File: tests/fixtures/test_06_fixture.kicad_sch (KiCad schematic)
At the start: 4 parts, among them SW1 Desc, SW2 Desc

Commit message: updated test 06 fixtures with LocLoad field
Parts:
- BT1: CInfo |(0,0,0)S40 -> (none); LocLoad (none) -> (0,0,0)S40
- FH1: CInfo |(10,0,0)R40 -> (none); LocLoad (none) -> (10,0,0)R40
- SW1: CInfo |(5,10,-2)R20 -> (none); LocLoad (none) -> (5,10,-2)R20
- SW2: CInfo |(5,10,2)R20 -> (none); LocLoad (none) -> (5,10,2)R20
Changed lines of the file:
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@@
 			)
 		)
-		(property "CInfo" "|(0,0,0)S40"
+		(property "LocLoad" "(0,0,0)S40"
 			(at 59.69 114.3 0)
 			(effects
@@
 			)
 		)
-		(property "CInfo" "|(5,10,-2)R20"
+		(property "LocLoad" "(5,10,-2)R20"
 			(at 138.43 53.34 0)
 			(effects
@@
 			)
 		)
-		(property "CInfo" "|(5,10,2)R20"
+		(property "LocLoad" "(5,10,2)R20"
 			(at 139.7 76.2 0)
 			(effects
@@
 		(dnp no)
 		(fields_autoplaced yes)
-		(property "Reference" "|(0,0,10)G"
+		(property "Reference" "GND"
 			(at 59.69 133.35 0)
 			(effects
@@
 		)
 		(property "Description" "Power symbol creates a global label with name \"GND\" , ground"
+			(at 59.69 127 0)
+			(effects
+				(font
+					(size 1.27 1.27)
+				)
+				(hide yes)
+			)
+		)
+		(property "LocLoad" "(0,0,10)G"
 			(at 59.69 127 0)
 			(effects
@@
 			(project ""
 				(path "/6f32b1c6-d0dc-4a69-b565-c121d7833096"
-					(reference "|(0,0,10)G")
+					(reference "GND")
 					(unit 1)
 				)
@@
 			)
 		)
-		(property "CInfo" "|(10,0,0)R40"
+		(property "LocLoad" "(10,0,0)R40"
 			(at 87.63 78.74 90)
 			(effects

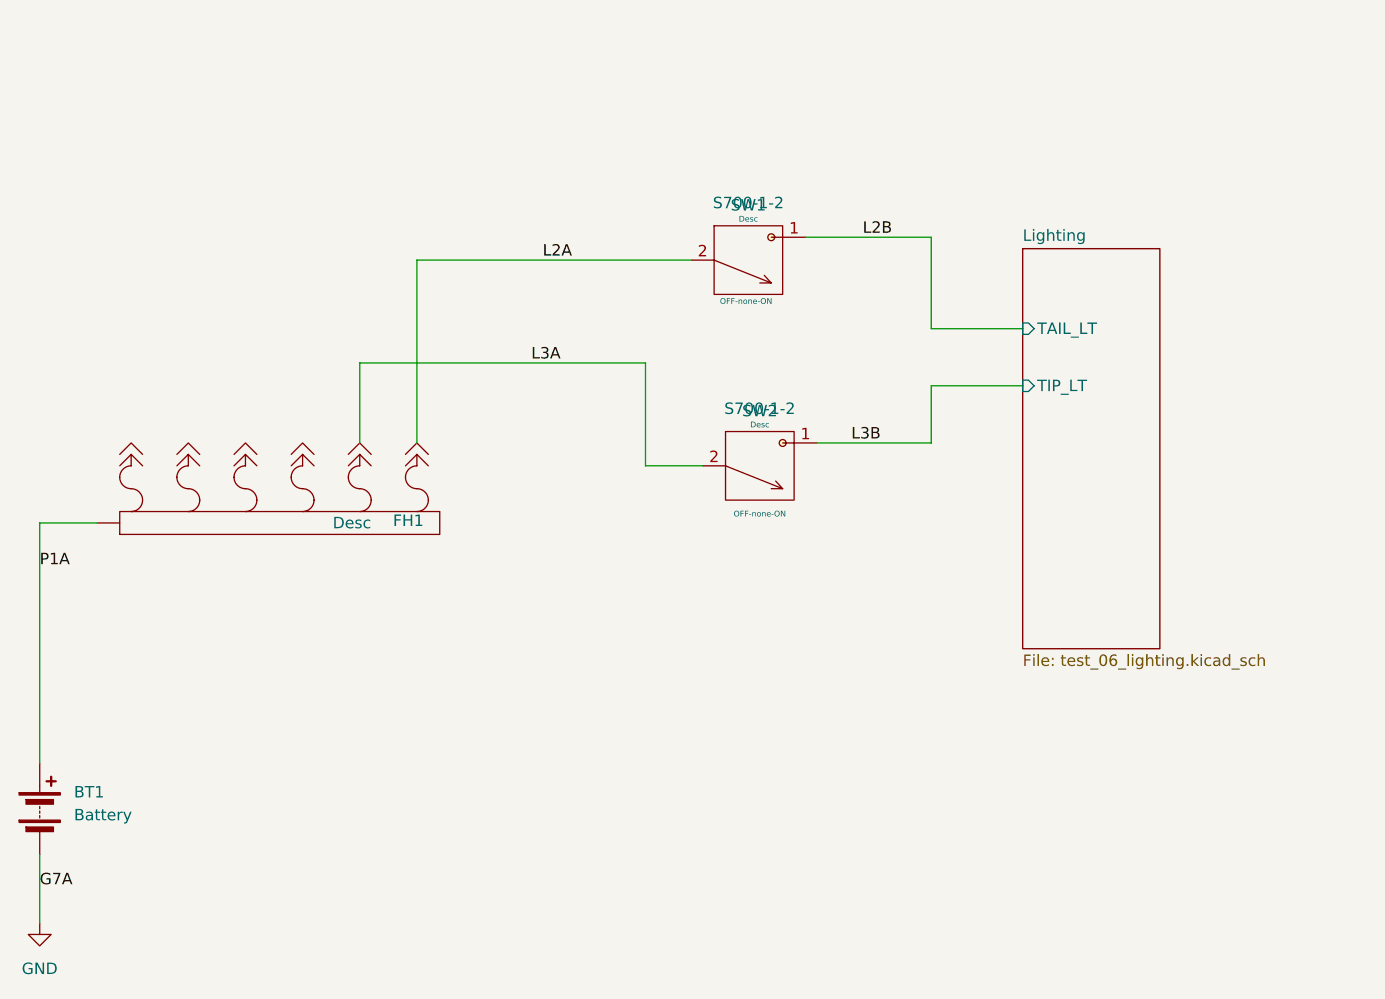
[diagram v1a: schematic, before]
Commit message: updated test_06 and added test_06 avionics. added "A" avionics to circuit types
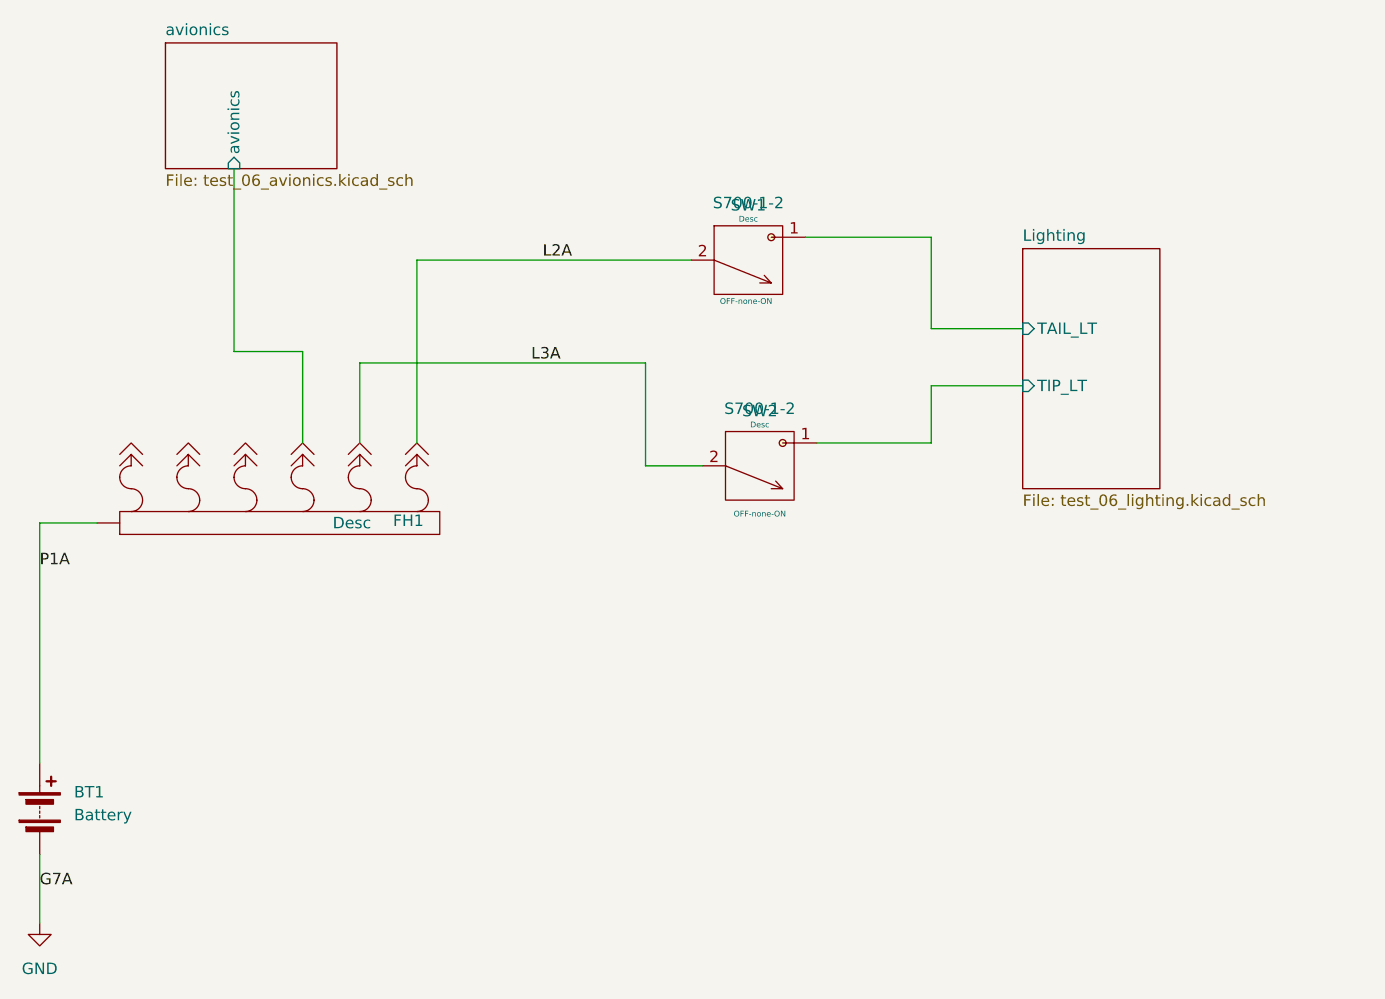
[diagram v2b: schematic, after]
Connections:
- net avionics/avionics: now reaches FH1.Val_A (Desc)
- net L2B renamed Lighting/TAIL_LT
- net L3B renamed Lighting/TIP_LT
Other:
- added sheet avionics (test_06_avionics.kicad_sch)
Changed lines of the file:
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@@
+	(wire
+		(pts
+			(xy 81.28 43.18) (xy 81.28 63.5)
+		)
+		(stroke
+			(width 0)
+			(type default)
+		)
+	)
+	(wire
+		(pts
+			(xy 88.9 63.5) (xy 88.9 73.66)
+		)
+		(stroke
+			(width 0)
+			(type default)
+		)
+	)
 	(wire
 		(pts
 			(xy 158.75 67.31) (xy 168.91 67.31)
+		)
+		(stroke
+			(width 0)
+			(type default)
+		)
+	)
+	(wire
+		(pts
+			(xy 81.28 63.5) (xy 88.9 63.5)
 		)
 		(stroke
@@
 		)
 	)
-	(label "L2B"
-		(at 151.13 50.8 0)
-		(effects
-			(font
-				(size 1.27 1.27)
-			)
-			(justify left bottom)
-		)
-	)
 	(label "L3A"
 		(at 114.3 64.77 0)
@@
 		)
 	)
-	(label "L3B"
-		(at 149.86 73.66 0)
-		(effects
-			(font
-				(size 1.27 1.27)
-			)
-			(justify left bottom)
-		)
-	)
 	(label "P1A"
 		(at 59.69 87.63 0)
@@
 	)
 	(sheet
-		(at 168.91 52.07)
-		(size 15.24 44.45)
+		(at 73.66 29.21)
+		(size 19.05 13.97)
 		(exclude_from_sim no)
 		(in_bom yes)
@@
 			(color 0 0 0 0.0000)
 		)
+		(property "Sheetname" "avionics"
+			(at 73.66 28.4984 0)
+			(effects
+				(font
+					(size 1.27 1.27)
+				)
+				(justify left bottom)
+			)
+		)
+		(property "Sheetfile" "test_06_avionics.kicad_sch"
+			(at 73.66 43.7646 0)
+			(effects
+				(font
+					(size 1.27 1.27)
+				)
+				(justify left top)
+			)
+		)
+		(pin "avionics" input
+			(at 81.28 43.18 270)
+			(effects
+				(font
+					(size 1.27 1.27)
+				)
+				(justify left)
+			)
+		)
+		(instances
+			(project "test_06_fixture"
+				(path "/6f32b1c6-d0dc-4a69-b565-c121d7833096"
+					(page "3")
+				)
+			)
+		)
+	)
+	(sheet
+		(at 168.91 52.07)
+		(size 15.24 26.67)
+		(exclude_from_sim no)
+		(in_bom yes)
+		(on_board yes)
+		(dnp no)
+		(fields_autoplaced yes)
+		(stroke
+			(width 0.1524)
+			(type solid)
+		)
+		(fill
+			(color 0 0 0 0.0000)
+		)
 		(property "Sheetname" "Lighting"
 			(at 168.91 51.3584 0)
@@
 		)
 		(property "Sheetfile" "test_06_lighting.kicad_sch"
-			(at 168.91 97.1046 0)
-			(effects
-				(font
+			(at 168.91 79.3246 0)
+			(effects
+				(font

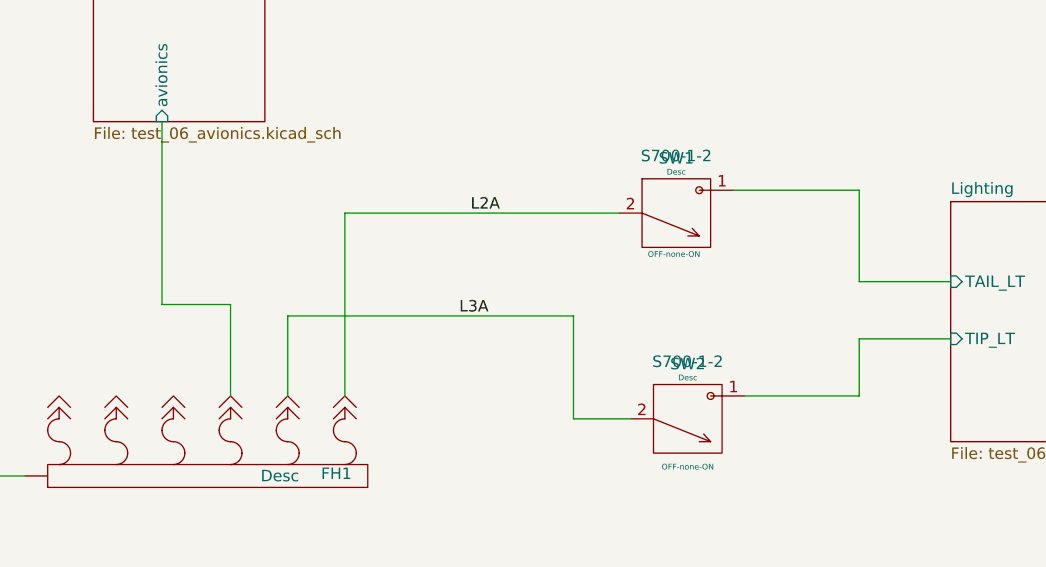
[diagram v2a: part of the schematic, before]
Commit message: updated fixtures to current methodology
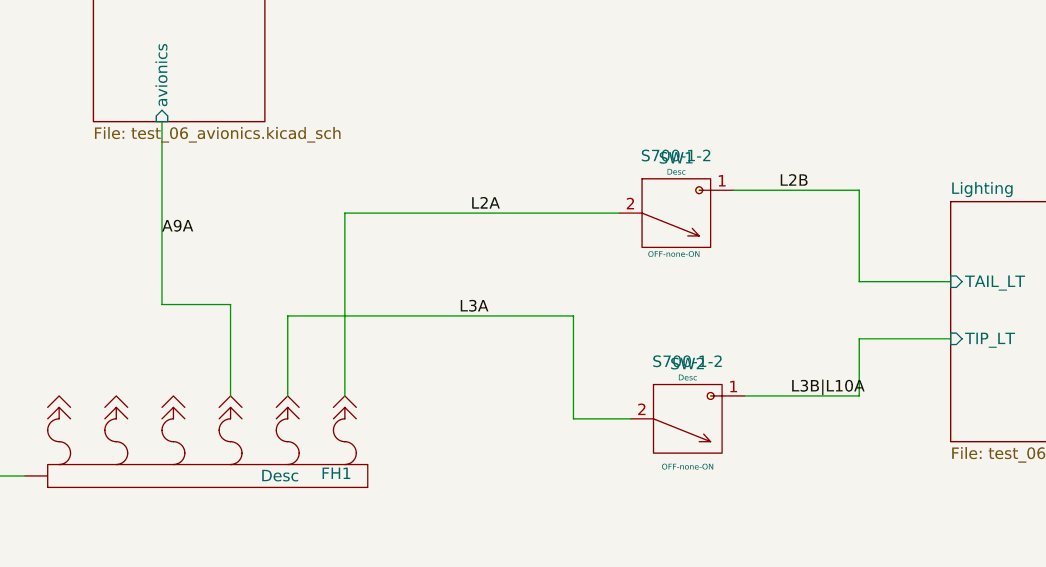
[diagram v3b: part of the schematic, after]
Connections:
- net avionics/avionics is gone; now on net L3A: FH1.Val_A (Desc)
- net Lighting/TAIL_LT renamed L2B
- net Lighting/TIP_LT renamed L3B|L10A
- new net A9A: FH1.Val_A (Desc)
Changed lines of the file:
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@@
+		)
+	)
+	(label "A9A"
+		(at 81.28 55.88 0)
+		(effects
+			(font
+				(size 1.27 1.27)
+			)
+			(justify left bottom)
 		)
 	)
@@
 	(label "L3A"
 		(at 114.3 64.77 0)
+		(effects
+			(font
+				(size 1.27 1.27)
+			)
+			(justify left bottom)
+		)
+	)
+	(label "L3B|L10A"
+		(at 151.13 73.66 0)
+		(effects
+			(font
+				(size 1.27 1.27)
+			)
+			(justify left bottom)
+		)
+	)
+	(label "L2B"
+		(at 149.86 50.8 0)
 		(effects
 			(font
@@
 		(dnp no)
 		(fields_autoplaced yes)
-		(property "Reference" "GND"
+		(property "Reference" "GND1"
 			(at 59.69 133.35 0)
 			(effects
@@
 			(project ""
 				(path "/6f32b1c6-d0dc-4a69-b565-c121d7833096"
-					(reference "GND")
+					(reference "GND1")
 					(unit 1)
 				)
